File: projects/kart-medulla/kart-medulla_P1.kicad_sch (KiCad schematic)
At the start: 62 parts, among them CN1 1990012, CN10 1990012, CN2 1990012, CN3 1990012, CN4 1990012, CN5 1990012, CN6 1990012, CN7 1990012, CN8 1990012, CN9 1990012, Q3 IRLZ44NPBF, Q4 BSS123_C5184436, U1 LM358DR, U13 MCP4922-E/SL, U14 MAX4660EUA+T, U19 L7805CDT_C20611927, U23 SSW-122-01-T-D, U24 SSW-122-01-T-S, U25 PCF8574T/3,518, U5 SN74LVC3G17DCTR

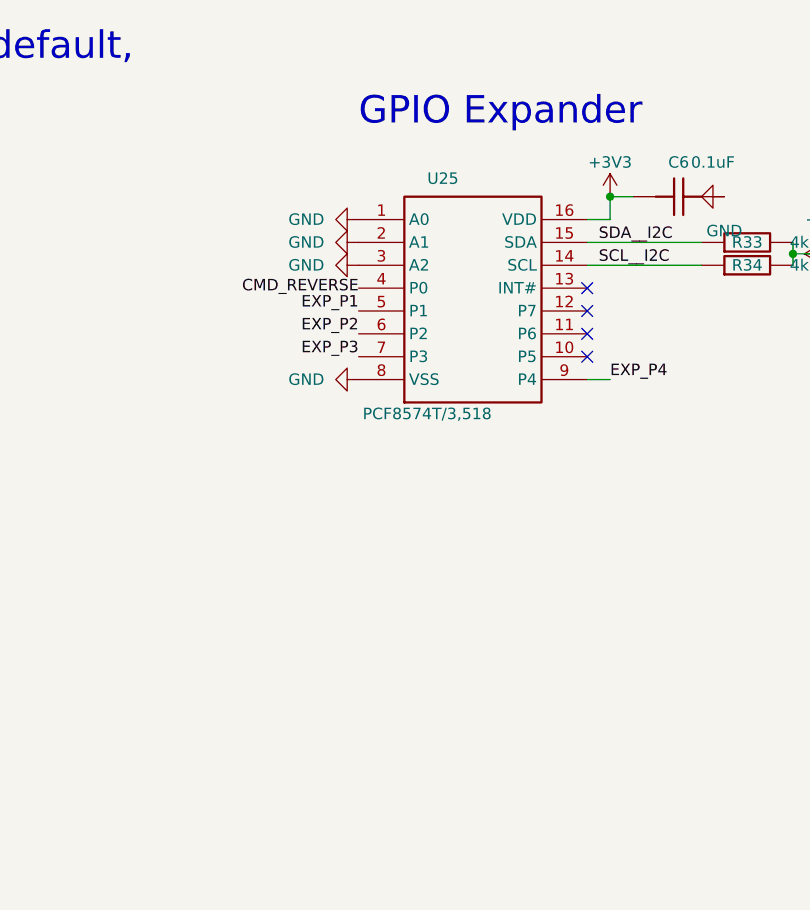
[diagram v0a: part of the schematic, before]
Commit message: add R35/R36: hold the DAC deselected when the ESP32 is unpowered
Audit finding. U13 (MCP4922) sits on +5V_REG, produced by the L7805 off +12V at CN1.2 -
a supply completely independent of the ESP32's. With the ESP32 in reset or being reflashed
its pins go high-impedance, so CS# floated with nothing driving it, and LDAC# is tied low
so there is no second latch: anything clocked in reaches VOUTB immediately. VOUTB has no
mux, unlike the throttle channel whose MAX4660 has a 10k pulldown defaulting to the pedal.
It goes through U1A x2 to CN10.2, the Festo VPPM pressure setpoint.

R35 = 10K from CMD_DAC_CS to +5V_REG, R36 = 10K from CLK to GND. The pull-up references
the DAC's own rail, not the ESP32's 3V3 - a pull-up to a rail that is off exactly when it
is needed does nothing.

ERC 0 violations, both confirmed on their intended nets in a fresh netlist export. Placed
in empty sheet space and checked by render: the first placement overlapped existing text
and the second was 60 mm off, which is not a multiple of the 1.27 mm grid, so ERC flagged
six off-grid endpoints.
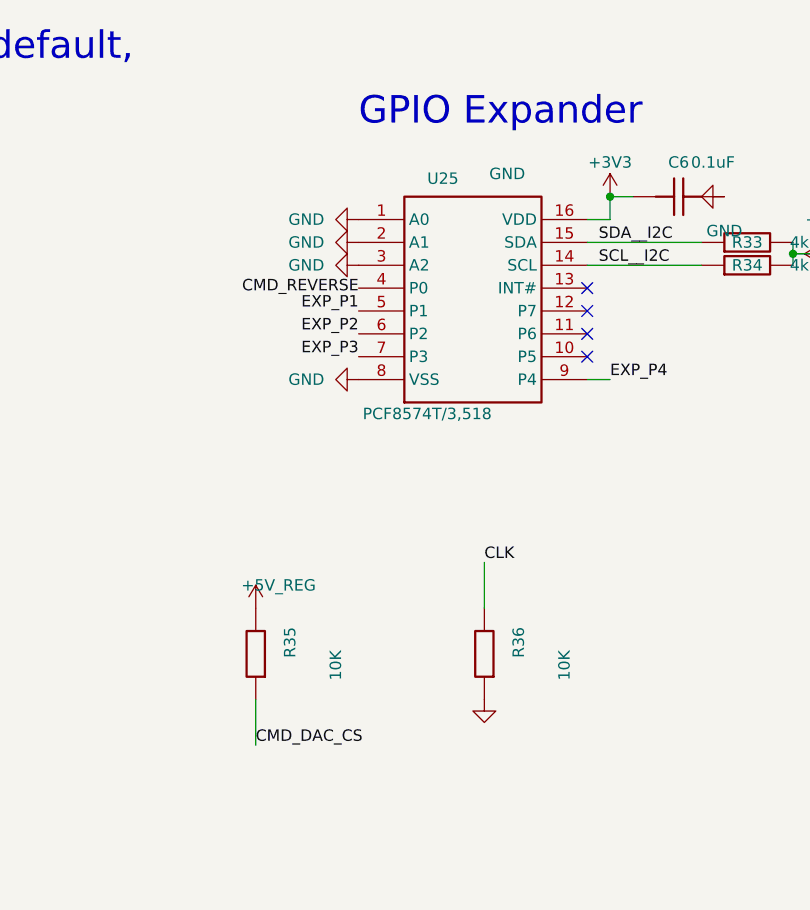
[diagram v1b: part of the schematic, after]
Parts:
- added R35, R36: 10K, kart-medulla:R0603, symbol kart-medulla:Res
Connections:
- net +5V_REG: now also R35.2
- net CLK: now also R36.2
- net CMD_DAC_CS: now also R35.1
- net GND: now also R36.1

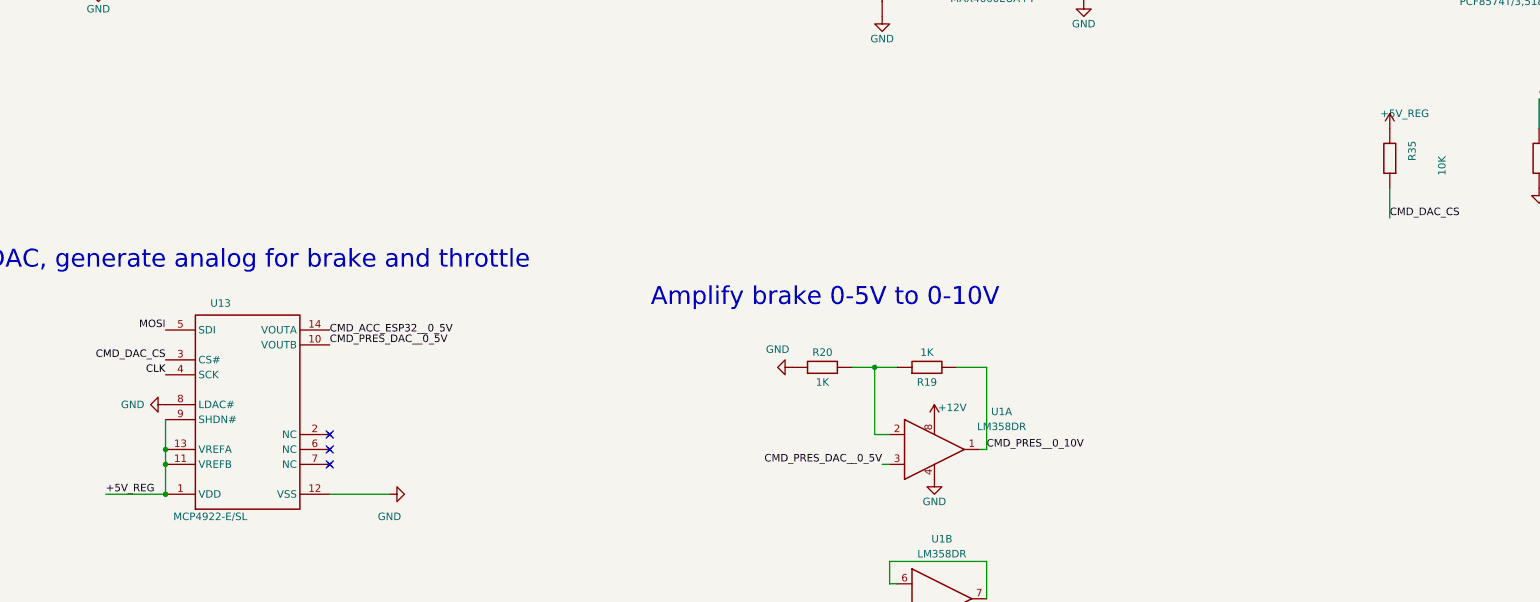
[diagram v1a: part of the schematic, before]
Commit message: move the MCP4922 to +3V3 and raise the amp gain to 3
Fixes the logic-level problem at its cause. Datasheet DS22250A p7: VIH min = 0.7 VDD for
all digital input pins - a fraction of the chosen supply, not an absolute, so VDD = 5 V made
the threshold 3.5 V that a 3.3 V ESP32 can never reach. At 3.3 V it is 2.31 V.

U13's VDD, SHDN#, VREFA and VREFB all tap one wire fed by a single label, so one label
change moves all four. Full scale drops ~4.96 V -> 3.3 V, so R19 goes 1K -> 2K for a gain of
3: 3.3 x 3 = 9.9 V at CN10.2, the same range as before since the LM358 only guarantees ~9 V
on 12 V anyway.

Also moved R35, the CS# pull-up added earlier today, from +5V_REG to +3V3. Pulling CS# to
5 V against a 3.3 V VDD exceeds absolute maximum VDD+0.3 and forward-biases the input
protection diode. A pull resistor follows the supply of the chip it holds.

Rejected the alternative of a 5 V HCT buffer in the SPI path - that patches a supply
decision with an extra part instead of correcting it.

Still open: CMD_ACC has no gain stage, so throttle reaches ~66% of the 0-5 V input at 3.3 V
full scale. The firmware repo's spi-fix branch already has a worked proposal (U1B at 1.52,
Rf 5.1k, lift U13 pin 14) which is not applied because U1B sits on the 12 V rail and would
feed a 5 V-supplied MAX4660.

ERC 0 violations.
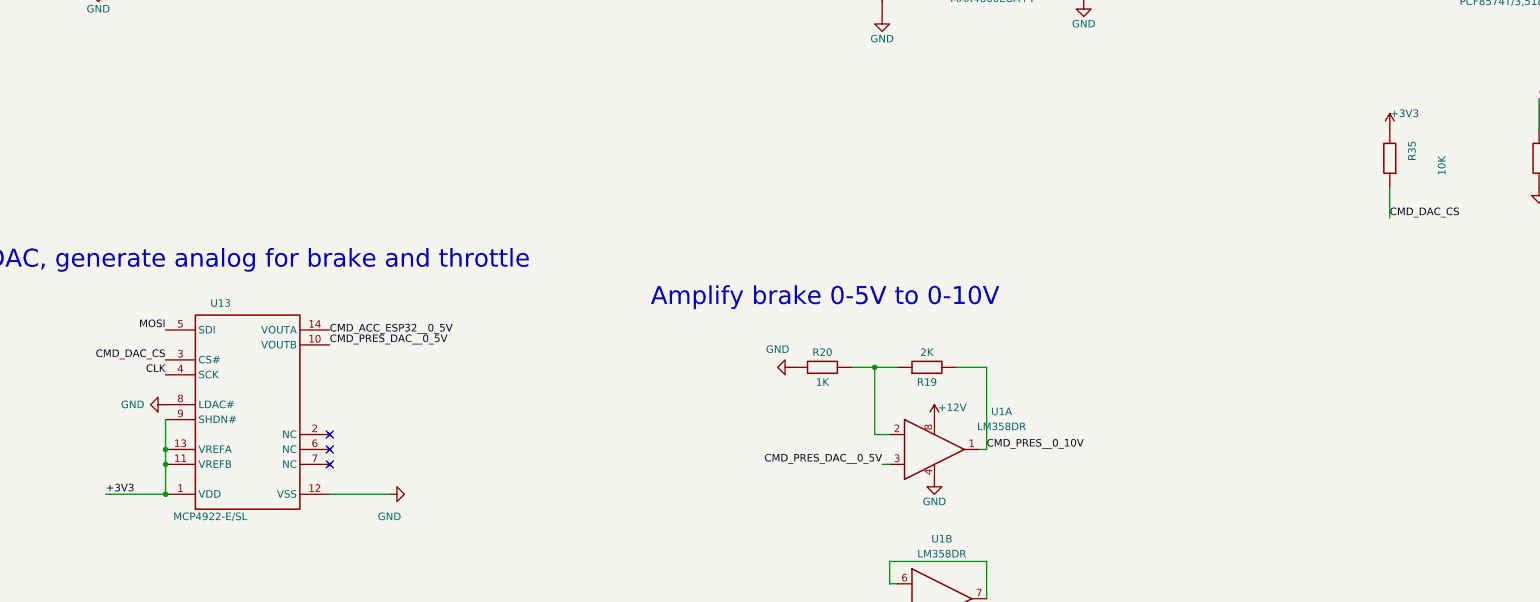
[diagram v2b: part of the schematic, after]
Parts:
- R19: value 1K -> 2K
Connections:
- net +3V3: now also R35.2, U13.1 (VDD), U13.11 (VREFB), U13.13 (VREFA), U13.9 (SHDN#)
- net +5V_REG: no longer R35.2, U13.1 (VDD), U13.11 (VREFB), U13.13 (VREFA), U13.9 (SHDN#)
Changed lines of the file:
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@@
 		)
 	)
-	(label "+5V_REG"
+	(label "+3V3"
 		(at 243.84 313.69 0)
 		(effects
@@
 			)
 		)
-		(property "Value" "1K"
+		(property "Value" "2K"
 			(at 383.54 289.56 0)
 			(show_name no)
@@
 	)
 	(symbol
-		(lib_id "kart-medulla:+5V_REG")
+		(lib_id "kart-medulla:+3V3")
 		(at 462.28 251.46 0)
 		(unit 1)
@@
 			)
 		)
-		(property "Value" "+5V_REG"
+		(property "Value" "+3V3"
 			(at 464.82 248.92 0)
 			(show_name no)

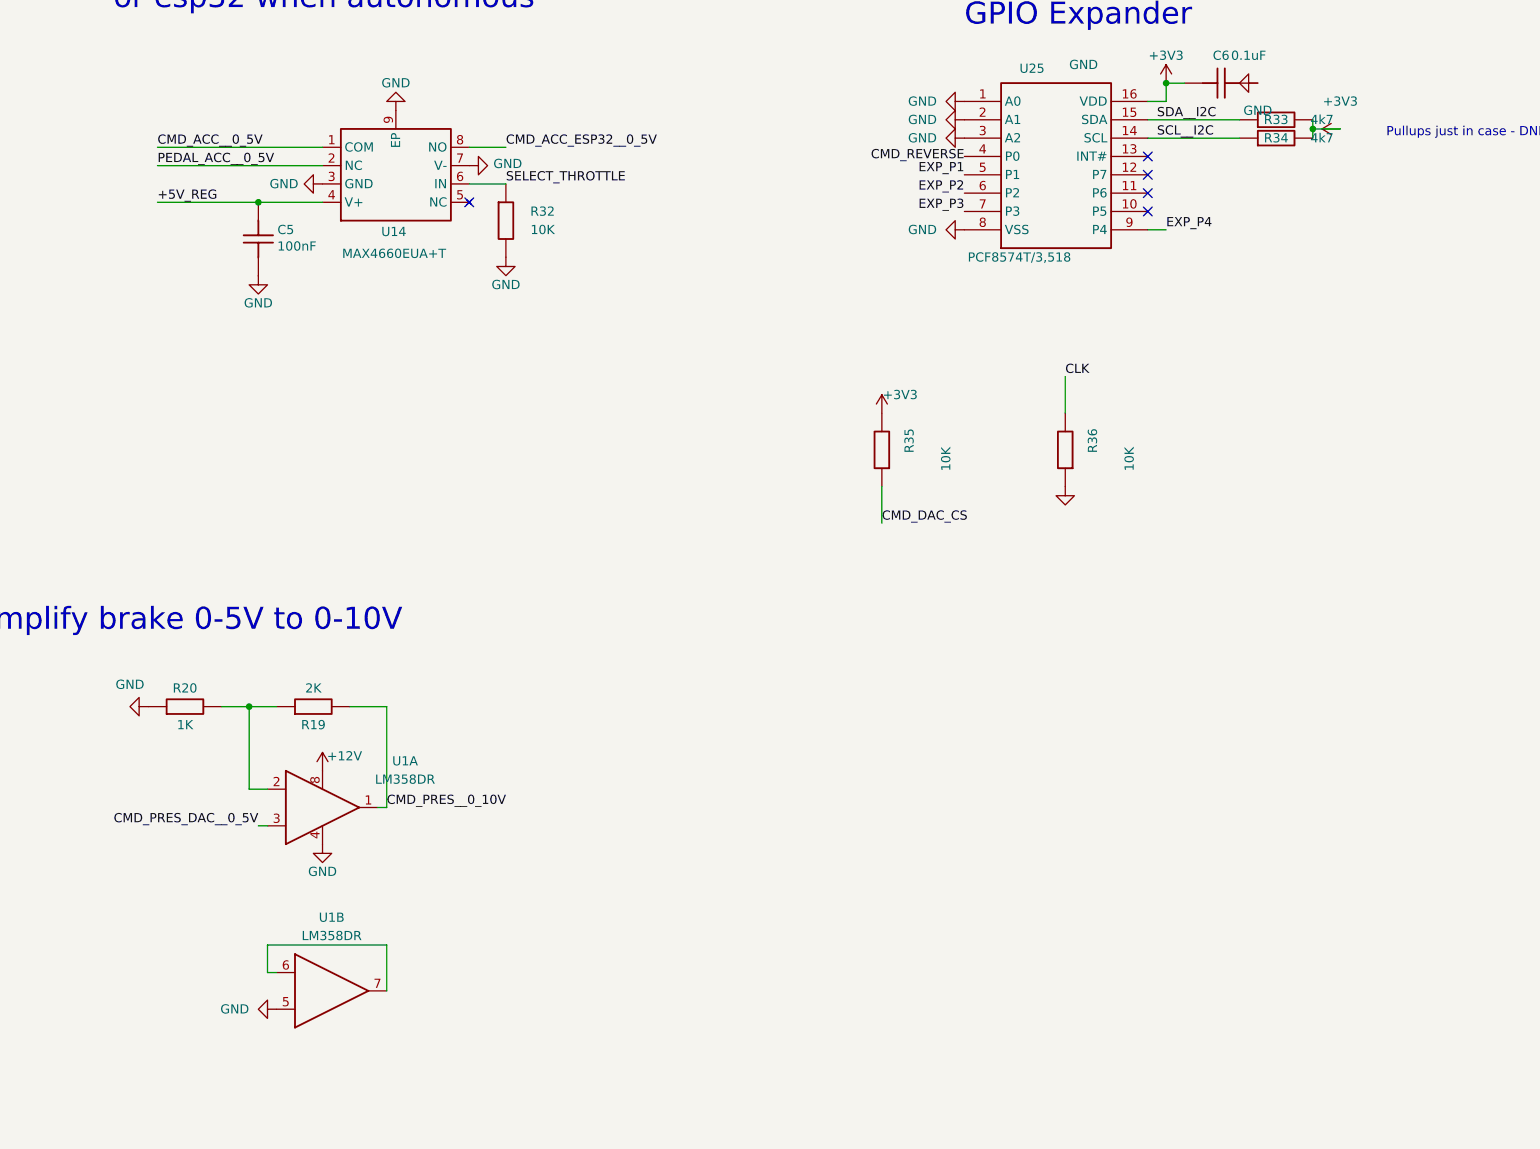
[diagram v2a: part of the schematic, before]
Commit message: wire U1B as the throttle gain stage, x1.51
Makes the 3.3 V DAC move free rather than a trade. U13 at +3V3 drops full scale to
3.3 V; the pressure path absorbed that with R19 1k->2k, but the throttle had no gain
stage at all and would have reached 66% of the motor controller's 0-5 V input.

U1B has been a parked follower since the design was drawn - input strapped to GND, output
looping to its own inverting pin. Now: VOUTA -> U1B x1.51 -> R39 -> U14.8 -> CN10.1.
R37 5.1k feedback, R38 10k to ground, 1 + 5.1/10 = 1.51, so 3.3 x 1.51 = 4.98 V. Full
range, no new IC. Same values the firmware repo's spi-fix branch derived for the PWM
bypass.

R39, the 1k in series, answers the objection I had raised against using U1B: it shares a
supply pin with U1A, which needs 12 V for the valve, so it sits on 12 V while the MAX4660
it feeds runs on 5 V. Normal operation cannot exceed 4.98 V because the input is a 3.3 V
DAC, so the resistor only matters if the op-amp saturates or the feedback opens - then it
limits current into the mux's clamp diodes instead of letting 12 V drive them.

Gain sits before the mux because the mux's other input is the pedal, already at 0-5 V.

ERC 0 violations, topology verified on a fresh netlist, both areas checked by render.
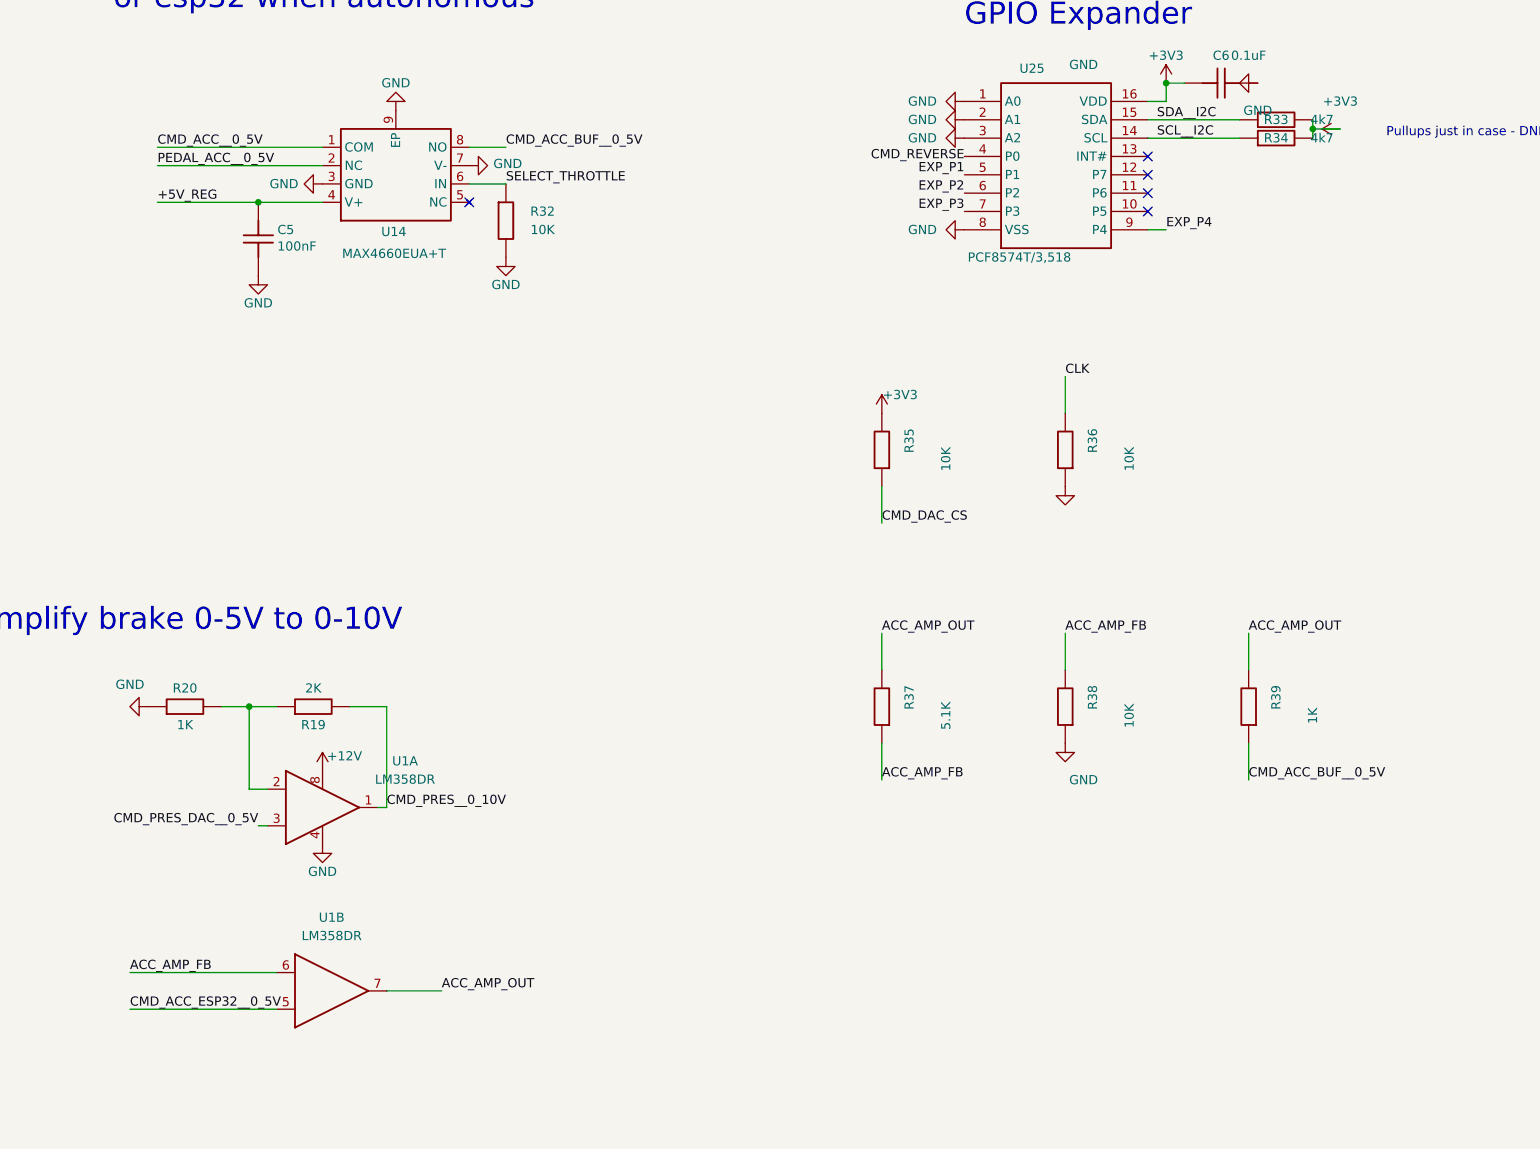
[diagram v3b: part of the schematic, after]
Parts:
- added R37: 5.1K, kart-medulla:R0603, symbol kart-medulla:Res
- added R38: 10K, kart-medulla:R0603, symbol kart-medulla:Res
- added R39: 1K, kart-medulla:R0603, symbol kart-medulla:Res
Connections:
- net CMD_ACC_ESP32__0_5V: now also U1.5 (+IN2); no longer U14.8 (NO)
- net GND: now also R38.1; no longer U1.5 (+IN2)
- net ACC_AMP_FB: now reaches U1.6 (-IN2)
- net ACC_AMP_FB: now also R37.1, R38.2; no longer U1.7 (OUT2)
- new net ACC_AMP_OUT: R37.2, R39.2, U1.7 (OUT2)
- new net CMD_ACC_BUF__0_5V: R39.1, U14.8 (NO)
